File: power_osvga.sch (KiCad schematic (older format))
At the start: 48 parts

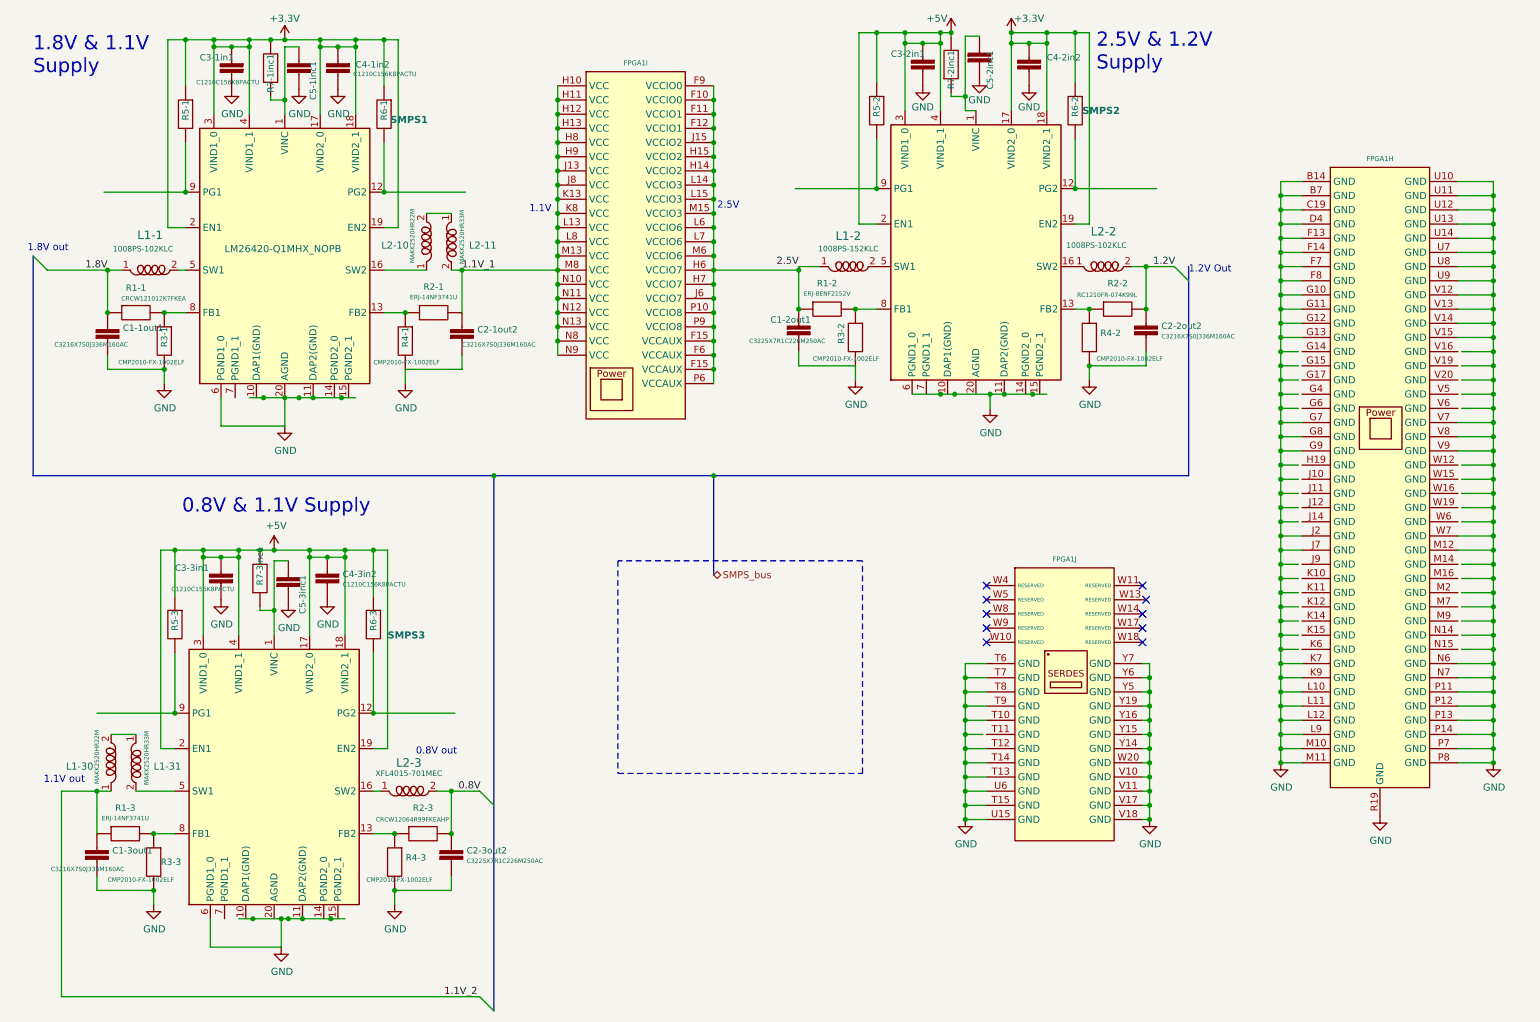
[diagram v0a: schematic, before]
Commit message: Add files via upload
Added Pull-up and pull-down resistors for JTAG and sysConfig connections.
Added pinheaders for FPGA-Configuration. (replacing edge-connector)
Combined the DVI+VGA and USB-C hierarchical sheets into one.
Assigned a dedicated sheet for the DAC.
Added 75 Ohm terminal-resistors to output of DAC.
Placed filtering-capacitors for DAC VAA.
Connected VGA ID-bits and DVI DDC together.
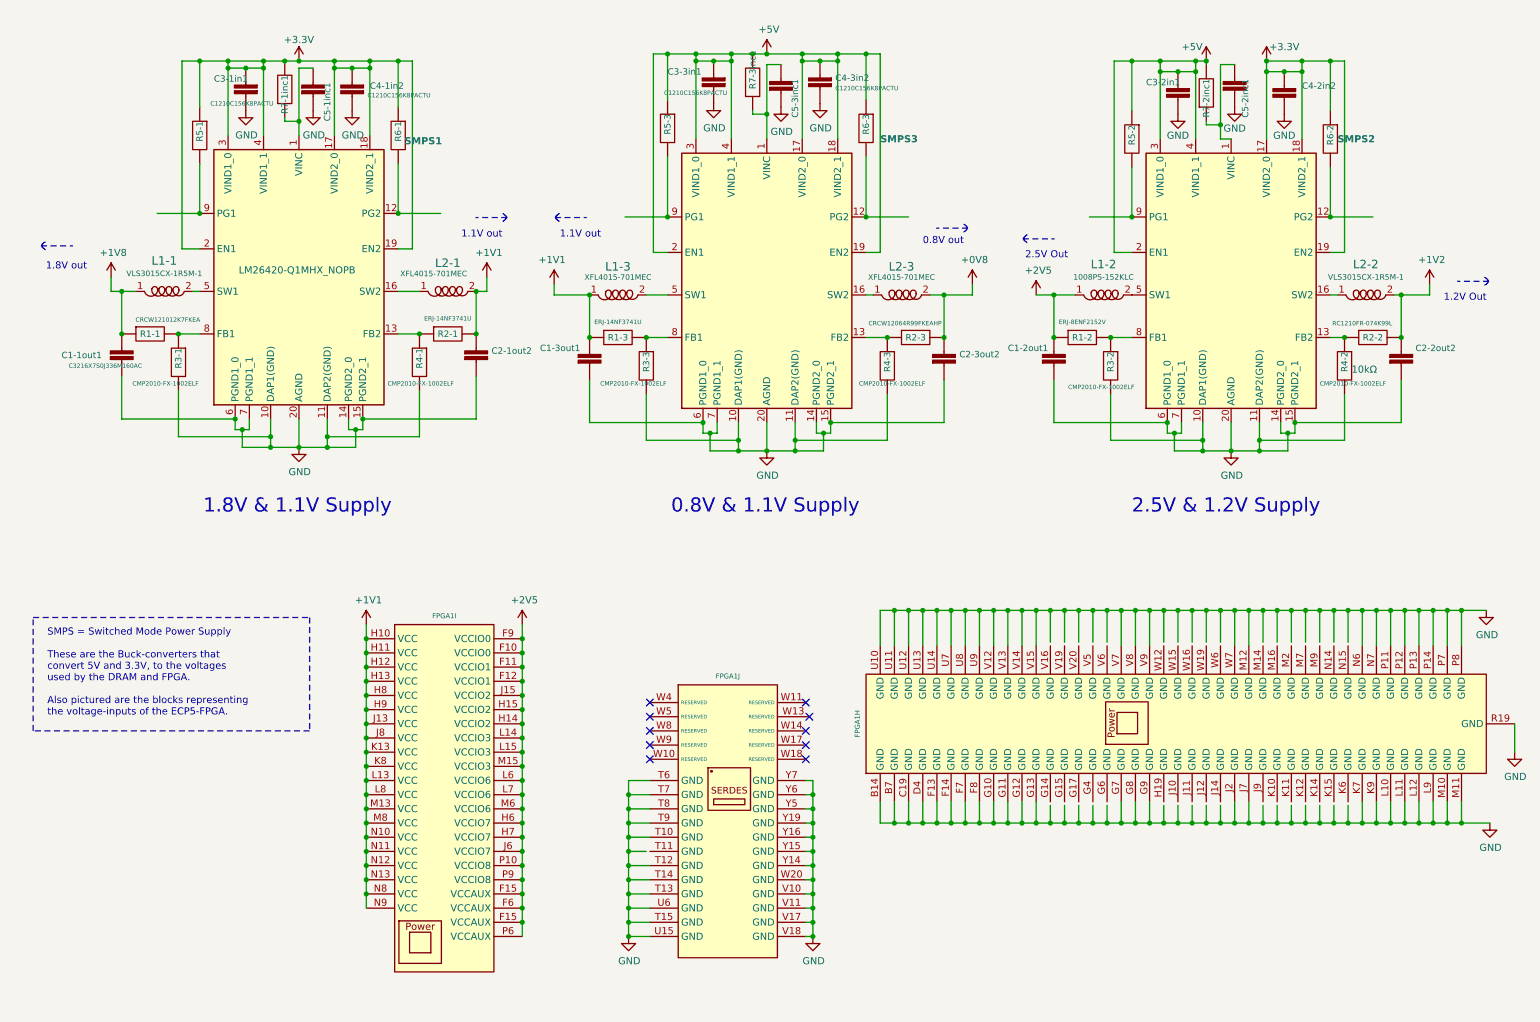
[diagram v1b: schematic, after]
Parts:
- removed L1-1, L2-2: 1008PS-102KLC, Inductor_SMD:L_1008_2520Metric, symbol LRJ-parts:1008PS-102KLC
- removed L1-30, L2-10: MAKK2520HR22M, Inductor_SMD:L_Taiyo-Yuden_MA-2520_HandSoldering, symbol LRJ-parts:MAKK2520HR22M
- removed L1-31, L2-11: MAKK2520HR33M, Inductor_SMD:L_Taiyo-Yuden_MA-2520_HandSoldering, symbol LRJ-parts:MAKK2520HR33M
- added L1-1, L2-2: VLS3015CX-1R5M-1, Inductor_SMD:L_TDK_VLS3015CX-1_handsoldering, symbol LRJ-parts:VLS3015CX-1R5M-1
- added L1-3, L2-1: XFL4015-701MEC, Inductor_SMD:L_Coilcraft_XFL4015, symbol LRJ-parts:XFL4015-701MEC
- R4-2: Value (none) -> 10kΩ
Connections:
- net labels added: +0V8, +1V1, +1V2, +1V8, +2V5
- net labels removed: 0.8V, 1.1V_1, 1.1V_2, 1.2V, 1.8V, 2.5V, SMPS_bus
- wire segments 436 -> 478
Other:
- note added: "1.8V & 1.1V Supply"
- note added: "2.5V & 1.2V Supply\n"
- note added: "2.5V Out"
- note added: "SMPS = Switched Mode Power Supply\n\nThese are the Buck-converters that \nconvert 5V and 3.3V, to the voltages \nused by the DRAM and FPGA.\n\nAlso pictured are the blocks representing \nthe voltage-inputs of the ECP5-FPGA."
- note removed: "1.1V"
- note removed: "1.8V & 1.1V \nSupply"
- note removed: "2.5V"
- note removed: "2.5V & 1.2V \nSupply\n"
- moved on the sheet: C1-1out1, C1-2out1, C1-3out1, C2-1out2, C2-2out2, C2-3out2, C3-1in1, C3-2in1, C3-3in1, C4-1in2, C4-2in2, C4-3in2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

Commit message: Add files via upload
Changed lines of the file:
@@
 $Descr A4 11693 8268
 encoding utf-8
-Sheet 7 9
+Sheet 5 9
 Title ""
 Date ""
@@
 	8875 850  8875 825
 Connection ~ 8875 825
-Wire Wire Line
-	1775 1550 1775 1900
 $Comp
 L LRJ-parts:RC1210FR-0749K9L R5-1
@@
 	10675 6200 10675 6050
 Wire Wire Line
-	7775 4925 7775 4700
-Wire Wire Line
-	7975 4925 7975 4700
+	7775 4950 7775 4700
+Wire Wire Line
+	7975 4950 7975 4700
 Wire Wire Line
 	10075 6200 10175 6200
@@
 Connection ~ 7775 6200
 Wire Wire Line
-	7775 6075 7775 6200
-Wire Wire Line
-	7875 6075 7875 6200
+	7775 6050 7775 6200
+Wire Wire Line
+	7875 6050 7875 6200
 Wire Wire Line
 	7775 6200 7875 6200
@@
 Connection ~ 7975 6200
 Wire Wire Line
-	7975 6075 7975 6200
+	7975 6050 7975 6200
 Wire Wire Line
 	7975 6200 8075 6200
 Connection ~ 8075 6200
 Wire Wire Line
-	8075 6075 8075 6200
-Wire Wire Line
-	8175 6075 8175 6200
+	8075 6050 8075 6200
+Wire Wire Line
+	8175 6050 8175 6200
 Wire Wire Line
 	8075 6200 8175 6200
@@
 Connection ~ 8575 6200
 Wire Wire Line
-	8575 6075 8575 6200
+	8575 6050 8575 6200
 Wire Wire Line
 	8575 6200 8675 6200
 Connection ~ 8675 6200
 Wire Wire Line
-	8675 6075 8675 6200
-Wire Wire Line
-	8775 6075 8775 6200
+	8675 6050 8675 6200
+Wire Wire Line
+	8775 6050 8775 6200
 Wire Wire Line
 	8675 6200 8775 6200
@@
 Connection ~ 8875 6200
 Wire Wire Line
-	8875 6075 8875 6200
+	8875 6050 8875 6200
 Wire Wire Line
 	8875 6200 8975 6200
 Connection ~ 8975 6200
 Wire Wire Line
-	8975 6075 8975 6200
+	8975 6050 8975 6200
 Wire Wire Line
 	9075 6050 9075 6200
@@
 Connection ~ 9275 6200
 Wire Wire Line
-	9275 6075 9275 6200
-Wire Wire Line
-	9375 6075 9375 6200
+	9275 6050 9275 6200
+Wire Wire Line
+	9375 6050 9375 6200
 Wire Wire Line
 	9275 6200 9375 6200
@@
 Connection ~ 9475 6200
 Wire Wire Line
-	9475 6075 9475 6200
+	9475 6050 9475 6200
 Wire Wire Line
 	9475 6200 9575 6200
 Connection ~ 9575 6200
 Wire Wire Line
-	9575 6075 9575 6200
-Wire Wire Line
-	9675 6075 9675 6200
+	9575 6050 9575 6200
+Wire Wire Line
+	9675 6050 9675 6200
 Wire Wire Line
 	9575 6200 9675 6200
@@
 Connection ~ 9775 6200
 Wire Wire Line
-	9775 6075 9775 6200
+	9775 6050 9775 6200
 Wire Wire Line
 	9775 6200 9875 6200
 Connection ~ 9875 6200
 Wire Wire Line
-	9875 6075 9875 6200
+	9875 6050 9875 6200
 Wire Wire Line
 	9875 6200 9975 6200
@@
 	9975 4950 9975 4700
 Wire Wire Line
-	9875 4925 9875 4700
+	9875 4950 9875 4700
 Connection ~ 9975 4700
 Connection ~ 9875 4700
@@
 	9875 4700 9975 4700
 Wire Wire Line
-	9775 4925 9775 4700
-Wire Wire Line
-	9675 4925 9675 4700
+	9775 4950 9775 4700
+Wire Wire Line
+	9675 4950 9675 4700
 Wire Wire Line
 	9775 4700 9875 4700
 Connection ~ 9775 4700
 Wire Wire Line
-	9575 4925 9575 4700
+	9575 4950 9575 4700
 Wire Wire Line
 	9675 4700 9775 4700
 Connection ~ 9675 4700
 Wire Wire Line
-	9475 4700 9475 4925
+	9475 4700 9475 4950
 Wire Wire Line
 	9575 4700 9675 4700
@@
 Connection ~ 9475 4700
 Wire Wire Line
-	9375 4700 9375 4925
-Wire Wire Line
-	9275 4700 9275 4925
+	9375 4700 9375 4950
+Wire Wire Line
+	9275 4700 9275 4950
 Wire Wire Line
 	9375 4700 9475 4700
@@
 Connection ~ 8975 4700
 Wire Wire Line
-	8975 4925 8975 4700
+	8975 4950 8975 4700
 Wire Wire Line
 	9075 4700 9175 4700
@@
 Connection ~ 9075 4700
 Wire Wire Line
-	8875 4925 8875 4700
-Wire Wire Line
-	8775 4925 8775 4700
-Wire Wire Line
-	8675 4925 8675 4700
+	8775 4950 8775 4700
+Wire Wire Line
+	8675 4950 8675 4700
 Connection ~ 8775 4700
 Wire Wire Line
@@
 Connection ~ 8675 4700
 Wire Wire Line
-	8575 4925 8575 4700
+	8575 4950 8575 4700
 Wire Wire Line
 	8475 4950 8475 4700
@@
 Connection ~ 8375 4700
 Wire Wire Line
-	8175 4925 8175 4700
+	8175 4950 8175 4700
 Wire Wire Line
 	8275 4700 8375 4700
@@
 Connection ~ 8175 4700
 Wire Wire Line
-	8075 4925 8075 4700
+	8075 4950 8075 4700
 Wire Wire Line
 	8775 4700 8875 4700
@@
 	7775 4700 7875 4700
 Wire Wire Line
-	7875 4925 7875 4700
+	7875 4950 7875 4700
 Connection ~ 7975 4700
 Connection ~ 7875 4700
@@
 	4950 6300 4800 6300
 Wire Wire Line
-	4925 6400 4800 6400
+	4950 6400 4800 6400
 Wire Wire Line
 	4950 6600 4800 6600
@@
 	3175 1900 3475 1900
 Connection ~ 3175 1900
-Connection ~ 1775 1900
 Wire Wire Line
 	4775 1925 5075 1925
@@
 Connection ~ 4800 6500
 Connection ~ 4800 6400
+Wire Wire Line
+	1775 1900 1775 1550
+Connection ~ 1775 1900
+Wire Wire Line
+	8875 4950 8875 4700
 $EndSCHEMATC
